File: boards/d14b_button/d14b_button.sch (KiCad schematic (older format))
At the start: 39 parts, among them SW1 SW_PUSH, SW2 SW_PUSH, U2 nRF24L01+-Module

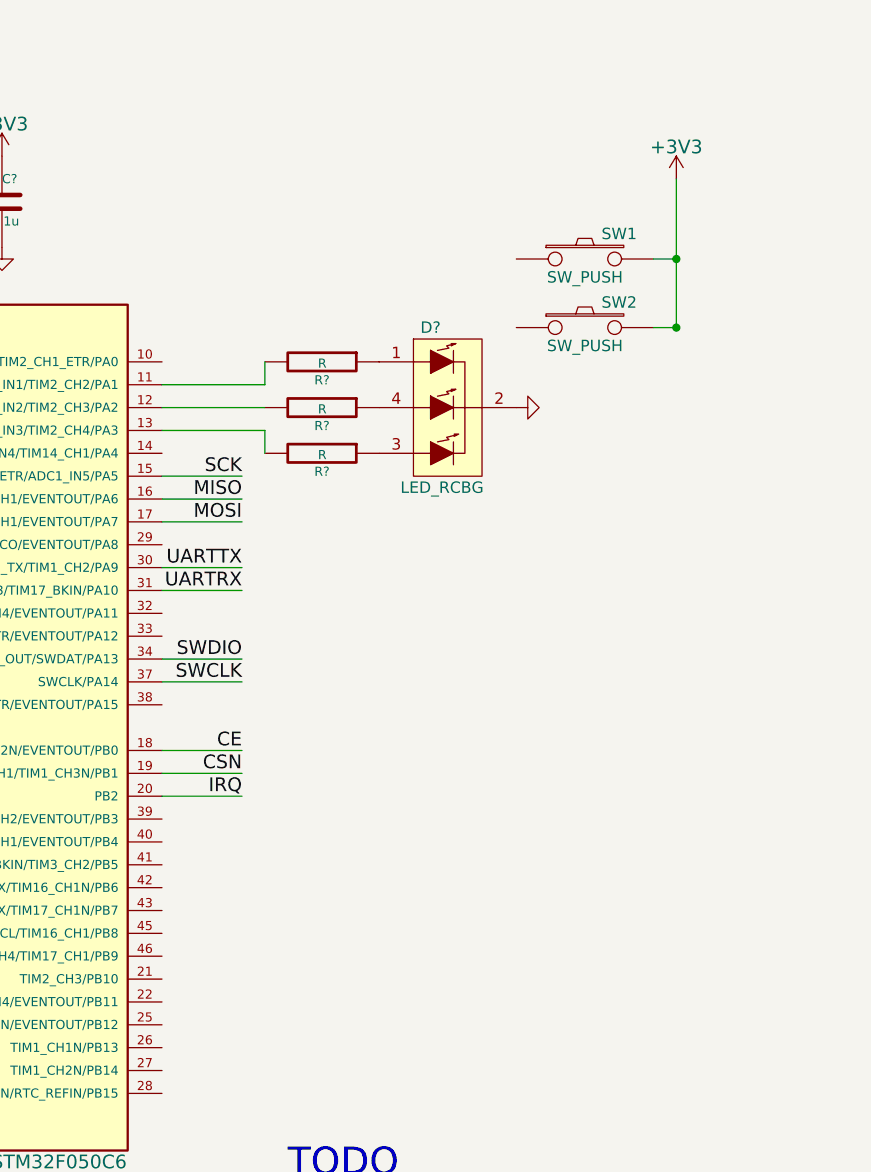
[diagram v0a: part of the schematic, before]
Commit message: dritten Schalter hinzugefügt und Annotation ausgeführt
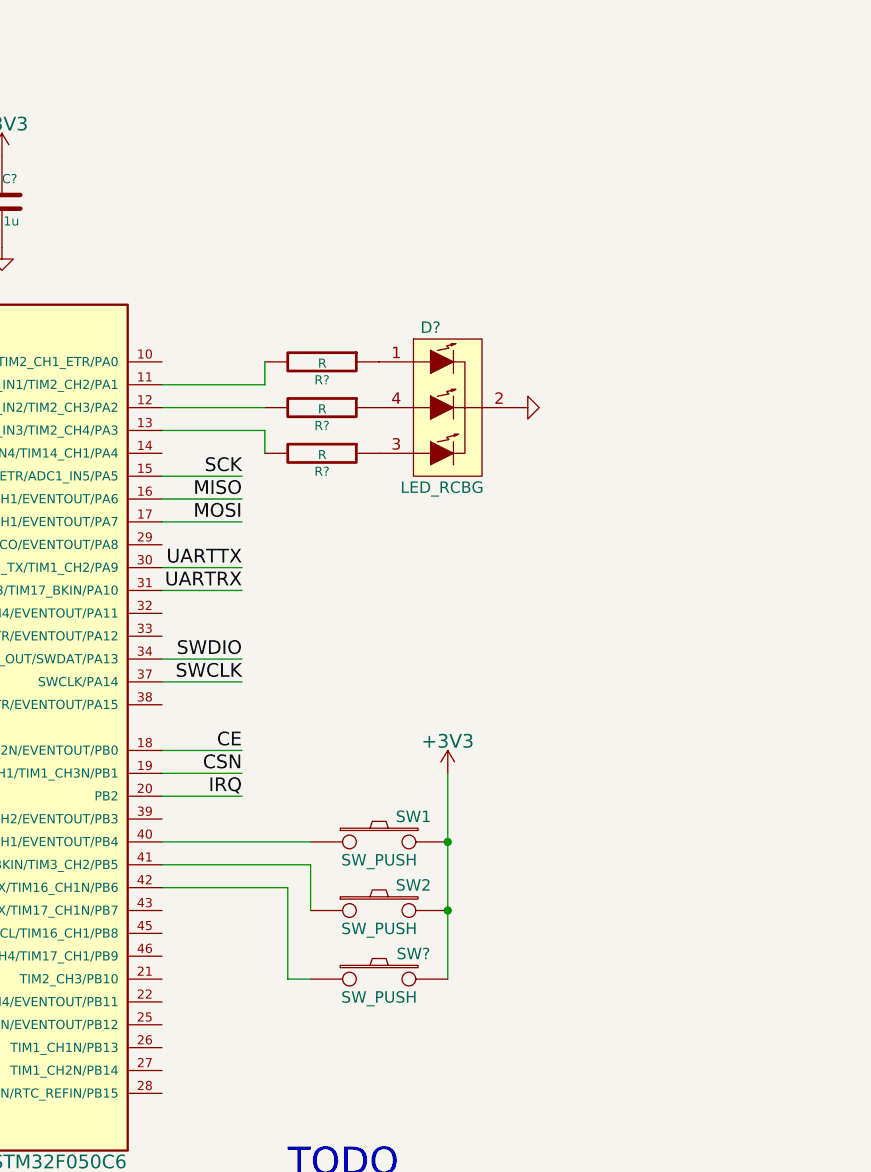
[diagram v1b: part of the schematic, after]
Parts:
- added SW?: SW_PUSH, d14b_libs:TACTILE_SW, symbol SW_PUSH
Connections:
- net +3V3: now also SW?.2
- net at SW1.1: now also U?.40 (SPI1_MISO/I2S1_MCK/TIM3_CH1/EVENTOUT/PB4)
- net at SW2.1: now also U?.41 (SPI1_MOSI/I2S1_SD/I2C1_SMBA/TIM16_BKIN/TIM3_CH2/PB5)
- net at U?.42 (I2C1_SCL/USART1_TX/TIM16_CH1N/PB6): now also SW?.1
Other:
- moved on the sheet: SW1, SW2
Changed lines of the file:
@@
 L SW_PUSH SW1
 U 1 1 5480667B
-P 6750 1600
-F 0 "SW1" H 6900 1710 50  0000 C CNN
-F 1 "SW_PUSH" H 6750 1520 50  0000 C CNN
-F 2 "d14b_libs:TACTILE_SW" H 6750 1600 60  0001 C CNN
-F 3 "" H 6750 1600 60  0000 C CNN
-	1    6750 1600
+P 5850 4150
+F 0 "SW1" H 6000 4260 50  0000 C CNN
+F 1 "SW_PUSH" H 5850 4070 50  0000 C CNN
+F 2 "d14b_libs:TACTILE_SW" H 5850 4150 60  0001 C CNN
+F 3 "" H 5850 4150 60  0000 C CNN
+	1    5850 4150
 	1    0    0    -1
 $EndComp
@@
 L SW_PUSH SW2
 U 1 1 548067BC
-P 6750 1900
-F 0 "SW2" H 6900 2010 50  0000 C CNN
-F 1 "SW_PUSH" H 6750 1820 50  0000 C CNN
-F 2 "d14b_libs:TACTILE_SW" H 6750 1900 60  0001 C CNN
-F 3 "" H 6750 1900 60  0000 C CNN
-	1    6750 1900
+P 5850 4450
+F 0 "SW2" H 6000 4560 50  0000 C CNN
+F 1 "SW_PUSH" H 5850 4370 50  0000 C CNN
+F 2 "d14b_libs:TACTILE_SW" H 5850 4450 60  0001 C CNN
+F 3 "" H 5850 4450 60  0000 C CNN
+	1    5850 4450
 	1    0    0    -1
 $EndComp
@@
 L +3V3 #PWR?
 U 1 1 54AFE5A1
-P 7150 1250
-F 0 "#PWR?" H 7150 1100 60  0001 C CNN
-F 1 "+3V3" H 7150 1390 60  0000 C CNN
-F 2 "" H 7150 1250 60  0000 C CNN
-F 3 "" H 7150 1250 60  0000 C CNN
-	1    7150 1250
+P 6150 3850
+F 0 "#PWR?" H 6150 3700 60  0001 C CNN
+F 1 "+3V3" H 6150 3990 60  0000 C CNN
+F 2 "" H 6150 3850 60  0000 C CNN
+F 3 "" H 6150 3850 60  0000 C CNN
+	1    6150 3850
 	1    0    0    -1
 $EndComp
@@
 	1    0    0    -1
 $EndComp
-Wire Wire Line
-	7050 1600 7150 1600
-Connection ~ 7150 1600
-Wire Wire Line
-	7150 1900 7050 1900
-Connection ~ 7150 1900
-Wire Wire Line
-	7150 1250 7150 1900
+Connection ~ 6150 4150
+Connection ~ 6150 4450
 Wire Wire Line
 	2900 6700 4050 6700
@@
 NoConn ~ 9250 4150
 NoConn ~ 9250 4250
+$Comp
+L SW_PUSH SW?
+U 1 1 54B0F915
+P 5850 4750
+F 0 "SW?" H 6000 4860 50  0000 C CNN
+F 1 "SW_PUSH" H 5850 4670 50  0000 C CNN
+F 2 "d14b_libs:TACTILE_SW" H 5850 4750 60  0001 C CNN
+F 3 "" H 5850 4750 60  0000 C CNN
+	1    5850 4750
+	1    0    0    -1
+$EndComp
+Wire Wire Line
+	6150 3850 6150 4750
+Wire Wire Line
+	4900 4150 5550 4150
+Wire Wire Line
+	4900 4250 5550 4250
+Wire Wire Line
+	5550 4250 5550 4450
+Wire Wire Line
+	4900 4350 5450 4350
+Wire Wire Line
+	5450 4350 5450 4750
+Wire Wire Line
+	5450 4750 5550 4750
 $EndSCHEMATC

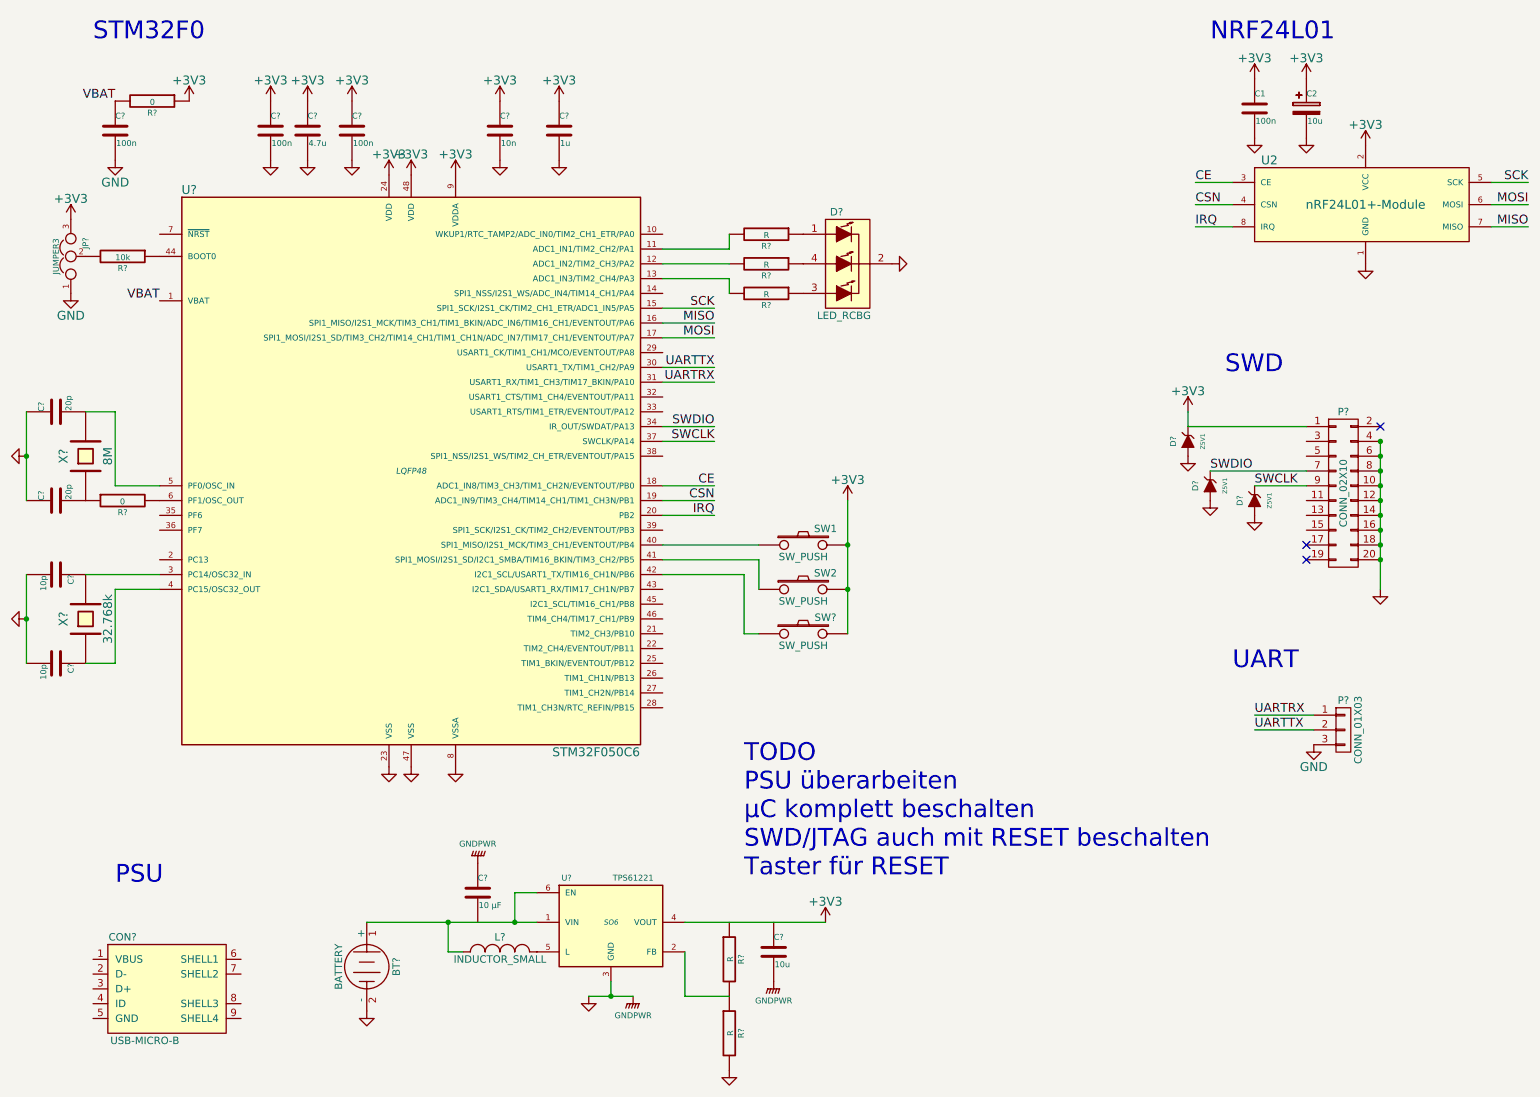
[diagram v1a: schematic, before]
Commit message: erste ERC-Runde durchgeführt
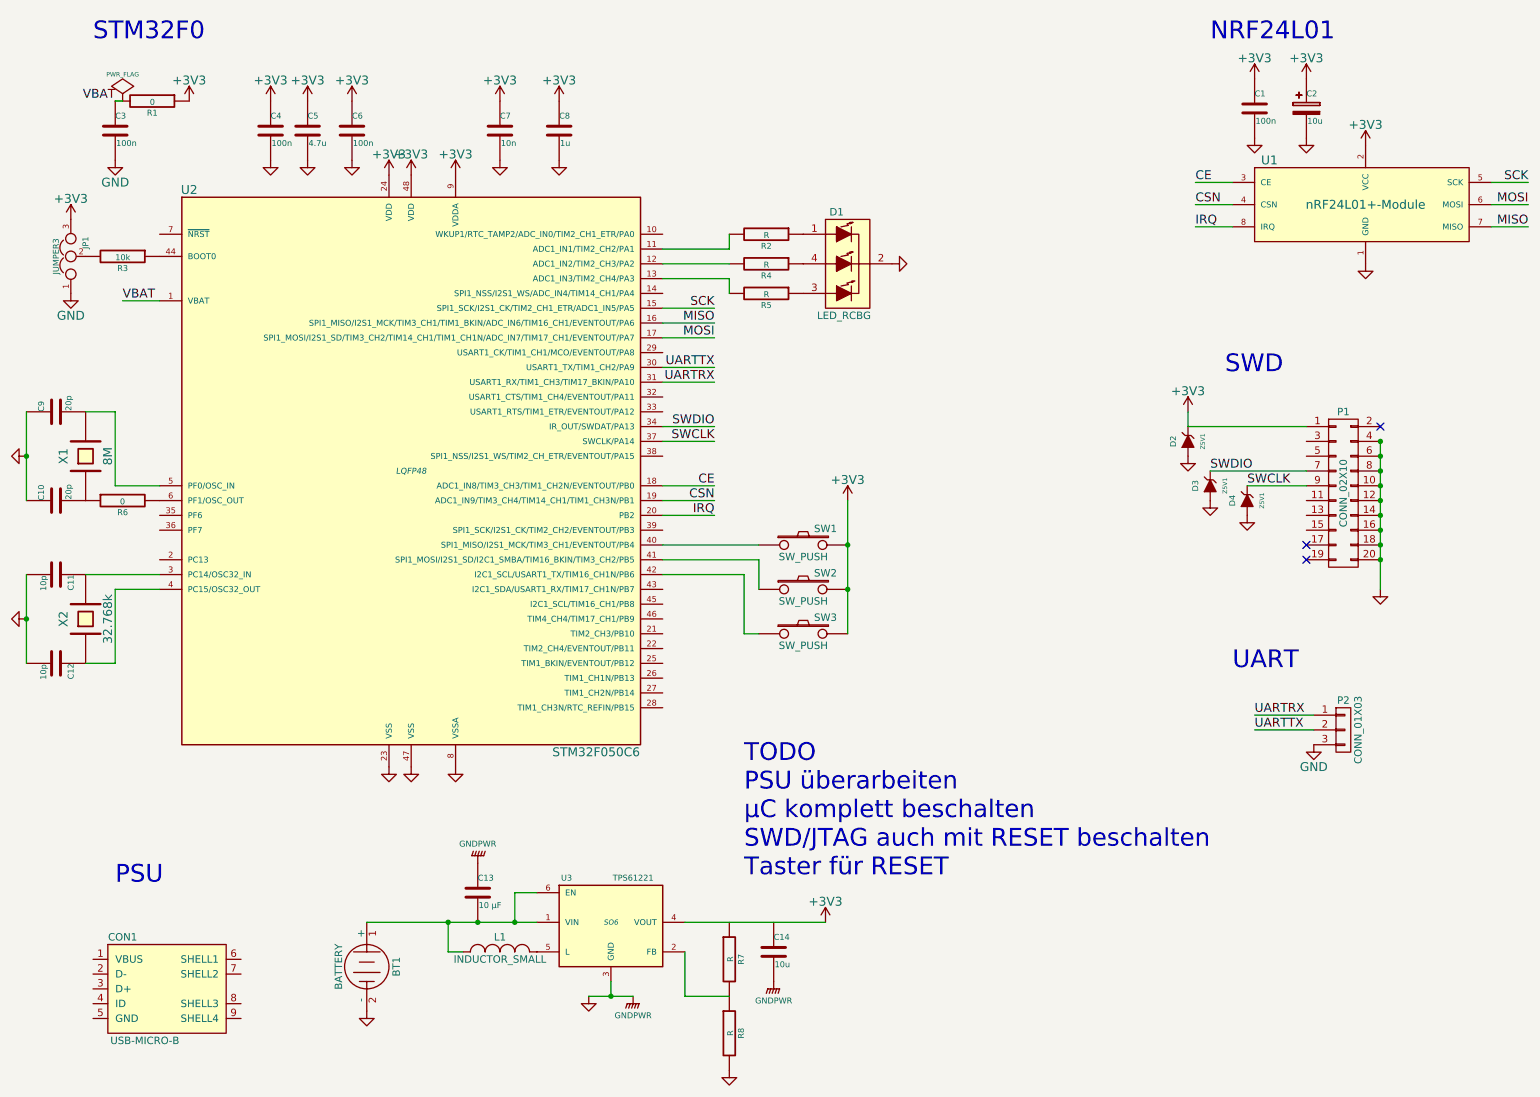
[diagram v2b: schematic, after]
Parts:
- gave numbers to parts that had none: 35
- renumbered U2 to U1
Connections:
- net at BT1.1 (+), L1.1, U3.1 (VIN)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: now also C13.2
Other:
- moved on the sheet: D4

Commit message: SWD verkabelt
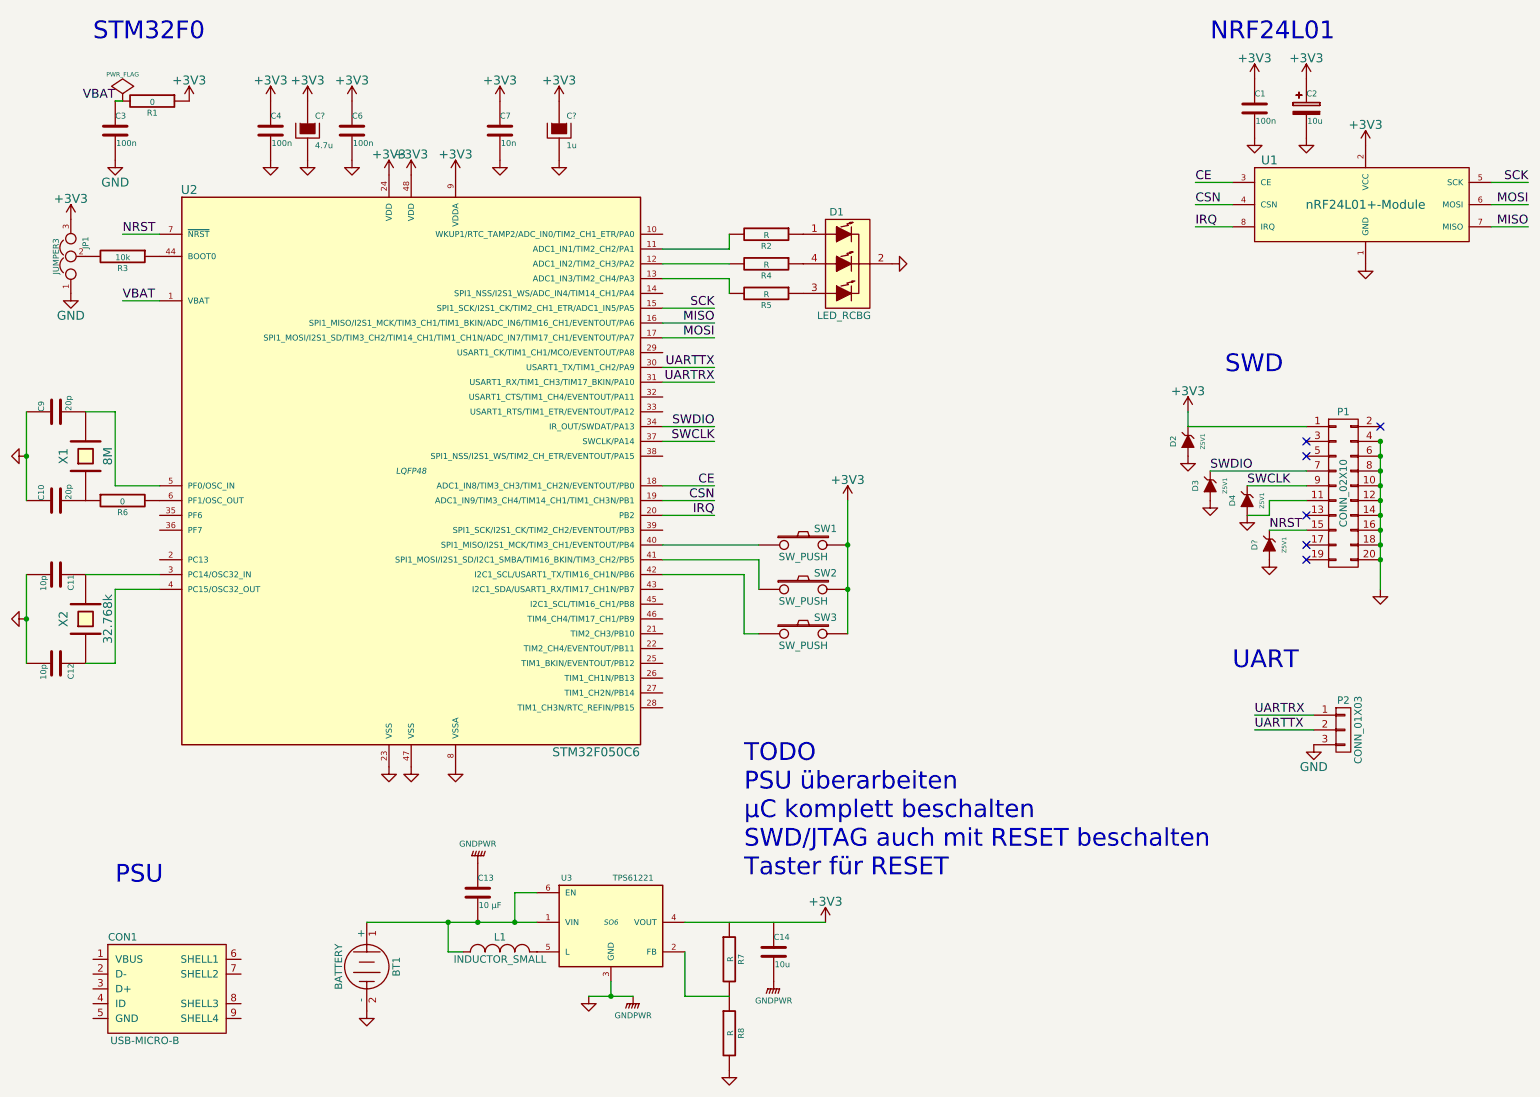
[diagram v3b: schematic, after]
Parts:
- removed C5: 4.7u, symbol C
- removed C8: 1u, symbol C
- added C?: 4.7u, symbol CAPAPOL
- added C?: 1u, symbol CAPAPOL
- added D?: Z5V1, symbol ZENERsmall
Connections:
- net +3V3: now also C?.1, C?.1
- net GND: now also P1.11 (P11), C?.2, C?.2, D?.1 (A)
- net NRST: now reaches P1.15 (P15)
- net NRST: now also U2.7 (~NRST), D?.2 (K)
- no-connect marks 3 -> 6
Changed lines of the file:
@@
-$EndComp
-$Comp
-L C C8
-U 1 1 54AF9C52
-P 4200 1350
-F 0 "C8" H 4200 1450 40  0000 L CNN
-F 1 "1u" H 4206 1265 40  0000 L CNN
-F 2 "" H 4238 1200 30  0000 C CNN
-F 3 "" H 4200 1350 60  0000 C CNN
-	1    4200 1350
-	1    0    0    -1
-$EndComp
-$Comp
-L C C5
-U 1 1 54AF9CB4
-P 2500 1350
-F 0 "C5" H 2500 1450 40  0000 L CNN
-F 1 "4.7u" H 2506 1265 40  0000 L CNN
-F 2 "" H 2538 1200 30  0000 C CNN
-F 3 "" H 2500 1350 60  0000 C CNN
-	1    2500 1350
-	1    0    0    -1
 $EndComp
 $Comp
@@
 Wire Wire Line
 	1250 1150 1200 1150
+Text Label 1250 2050 0    60   ~ 0
+NRST
+Wire Wire Line
+	1500 2050 1250 2050
+Text Label 9000 4050 0    60   ~ 0
+NRST
+$Comp
+L ZENERsmall D?
+U 1 1 54B1B9F1
+P 9000 4150
+F 0 "D?" H 9000 4250 40  0000 C CNN
+F 1 "Z5V1" H 9000 4050 30  0000 C CNN
+F 2 "" H 9000 4150 60  0000 C CNN
+F 3 "" H 9000 4150 60  0000 C CNN
+	1    9000 4150
+	0    -1   -1   0
+$EndComp
+$Comp
+L GND #PWR?
+U 1 1 54B1B9F7
+P 9000 4250
+F 0 "#PWR?" H 9000 4250 30  0001 C CNN
+F 1 "GND" H 9000 4180 30  0001 C CNN
+F 2 "" H 9000 4250 60  0000 C CNN
+F 3 "" H 9000 4250 60  0000 C CNN
+	1    9000 4250
+	1    0    0    -1
+$EndComp
+Wire Wire Line
+	9000 4050 9250 4050
+Wire Wire Line
+	9250 3850 9000 3850
+Wire Wire Line
+	9000 3850 9000 3950
+Wire Wire Line
+	9000 3950 8850 3950
+$Comp
+L CAPAPOL C?
+U 1 1 54B1C241
+P 2500 1350
+F 0 "C?" H 2550 1450 40  0000 L CNN
+F 1 "4.7u" H 2550 1250 40  0000 L CNN
+F 2 "" H 2600 1200 30  0000 C CNN
+F 3 "" H 2500 1350 300 0000 C CNN
+	1    2500 1350
+	1    0    0    -1
+$EndComp
+$Comp
+L CAPAPOL C?
+U 1 1 54B1C439
+P 4200 1350
+F 0 "C?" H 4250 1450 40  0000 L CNN
+F 1 "1u" H 4250 1250 40  0000 L CNN
+F 2 "" H 4300 1200 30  0000 C CNN
+F 3 "" H 4200 1350 300 0000 C CNN
+	1    4200 1350
+	1    0    0    -1
+$EndComp
+NoConn ~ 9250 3950
+NoConn ~ 9250 3450
+NoConn ~ 9250 3550
 $EndSCHEMATC
